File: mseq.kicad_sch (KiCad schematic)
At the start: 63 parts, among them J1 Conn_01x04_Pin, J2 TC2030-NL, P1 USB_C_Plug_USB2.0, SW1 SW_SPST, SW2 BOOT, SW3 RESET, SW4 SW_SPST, U2 SN74AHCT125DR, U3 MIC5219-3.3YM5, U4 CP2102N-Axx-xQFN20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

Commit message: MPN added
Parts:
- C20: footprint Capacitor_SMD:C_0201_0603Metric -> Capacitor_SMD:C_0603_1608Metric; MPN (none) -> KGM15BR71A105JT; voltage rating (none) -> 10
- C4: footprint Capacitor_SMD:C_0201_0603Metric -> Capacitor_SMD:C_0603_1608Metric; MPN (none) -> 0603ZC104JAT2A; Voltage (none) -> 10
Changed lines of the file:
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@@
 			)
 		)
-		(property "Footprint" "Capacitor_SMD:C_0201_0603Metric"
+		(property "Footprint" "Capacitor_SMD:C_0603_1608Metric"
 			(at 97.4852 212.09 0)
 			(effects
@@
 			)
 		)
+		(property "MPN" "0603ZC104JAT2A "
+			(at 96.52 208.28 0)
+			(effects
+				(font
+					(size 1.27 1.27)
+				)
+				(hide yes)
+			)
+		)
+		(property "Voltage" "10"
+			(at 96.52 208.28 0)
+			(effects
+				(font
+					(size 1.27 1.27)
+				)
+				(hide yes)
+			)
+		)
 		(pin "1"
 		)
@@
 			)
 		)
-		(property "Footprint" "Capacitor_SMD:C_0201_0603Metric"
+		(property "Footprint" "Capacitor_SMD:C_0603_1608Metric"
 			(at 86.0552 212.09 0)
 			(effects
@@
 			(at 85.09 208.28 0)
 			(effects
+				(font
+					(size 1.27 1.27)
+				)
+				(hide yes)
+			)
+		)
+		(property "MPN" "KGM15BR71A105JT "
+			(at 85.09 208.28 0)
+			(effects
+				(font
+					(size 1.27 1.27)
+				)
+				(hide yes)
+			)
+		)
+		(property "voltage rating" "10"
+			(at 85.09 208.28 0)
+			(effects

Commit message: MPN capacitor almost done
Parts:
- removed U3: MIC5219-3.3YM5, Package_TO_SOT_SMD:SOT-23-5, symbol Regulator_Linear:MIC5219-3.3YM5
- added U3: MCP1703Ax-330xxTT, Package_TO_SOT_SMD:SOT-23, symbol Regulator_Linear:MCP1703Ax-330xxTT
- C1, C10, C11, C14, C2, C3, C5, C8: footprint Capacitor_SMD:C_0201_0603Metric -> Capacitor_SMD:C_0603_1608Metric; MPN (none) -> 0603ZC104JAT2A; Voltage (none) -> 10
- C21: footprint Capacitor_SMD:C_0201_0603Metric -> Capacitor_SMD:C_0603_1608Metric; MPN (none) -> KAF15AR71H103JM; Voltage (none) -> 50
- C6, C7: value 4.7uF -> 1uF
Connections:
- net BOOT0: now also C8.1; no longer C8.2
- net GND: now also C11.1, C5.2, C8.2, U3.1 (GND); no longer C11.2, C5.1, C8.1
- net NRST: now also C11.2; no longer C5.2
- net VBAT: now also U3.2 (VO)
- net VBUS: now also U3.3 (VI)
- net VDD3: now also C5.1; no longer C11.1
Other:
- moved on the sheet: C7, C9

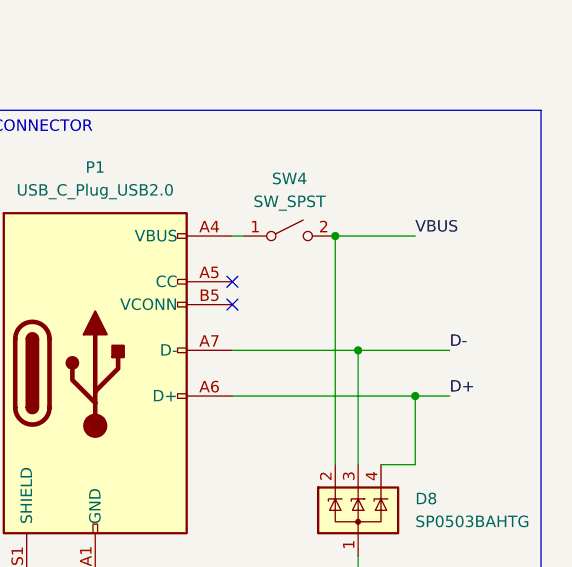
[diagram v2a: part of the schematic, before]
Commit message: Bypass capacitor in VCC don
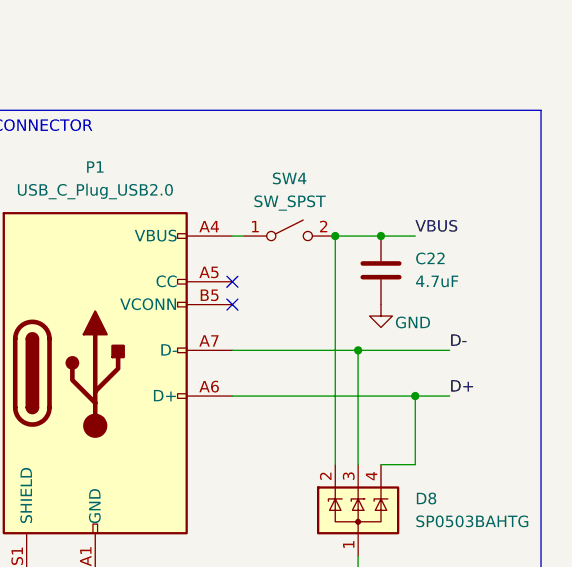
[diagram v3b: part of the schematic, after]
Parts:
- added C22: 4.7uF, Capacitor_SMD:C_0201_0603Metric, symbol Device:C
- C7: footprint Capacitor_SMD:C_0201_0603Metric -> Capacitor_SMD:C_0603_1608Metric; MPN (none) -> KGM15BR71C105JT; Voltage (none) -> 16
- C9: footprint Capacitor_SMD:C_0201_0603Metric -> Capacitor_SMD:C_0603_1608Metric; MPN (none) -> KGM15AR71C103JT; Voltage (none) -> 16
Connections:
- net GND: now also C22.2
- net VBUS: now also C22.1
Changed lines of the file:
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@@
 	)
 	(junction
+		(at 387.35 200.66)
+		(diameter 0)
+		(color 0 0 0 0)
+	)
+	(junction
 		(at 220.98 212.09)
 		(diameter 0)
@@
 	(wire
 		(pts
-			(xy 382.27 200.66) (xy 391.16 200.66)
+			(xy 382.27 200.66) (xy 387.35 200.66)
 		)
 		(stroke
@@
 	(wire
 		(pts
+			(xy 387.35 200.66) (xy 391.16 200.66)
+		)
+		(stroke
+			(width 0)
+			(type default)
+		)
+	)
+	(wire
+		(pts
 			(xy 46.99 160.02) (xy 58.42 160.02)
 		)
@@
 	)
 	(symbol
+		(lib_id "Device:C")
+		(at 387.35 204.47 0)
+		(unit 1)
+		(exclude_from_sim no)
+		(in_bom yes)
+		(on_board yes)
+		(dnp no)
+		(property "Reference" "C22"
+			(at 391.16 203.1999 0)
+			(effects
+				(font
+					(size 1.27 1.27)
+				)
+				(justify left)
+			)
+		)
+		(property "Value" "4.7uF"
+			(at 391.16 205.7399 0)
+			(effects
+				(font
+					(size 1.27 1.27)
+				)
+				(justify left)
+			)
+		)
+		(property "Footprint" "Capacitor_SMD:C_0201_0603Metric"
+			(at 388.3152 208.28 0)
+			(effects
+				(font
+					(size 1.27 1.27)
+				)
+				(hide yes)
+			)
+		)
+		(property "Datasheet" "~"
+			(at 387.35 204.47 0)
+			(effects
+				(font
+					(size 1.27 1.27)
+				)
+				(hide yes)
+			)
+		)
+		(property "Description" "Unpolarized capacitor"
+			(at 387.35 204.47 0)
+			(effects
+				(font
+					(size 1.27 1.27)
+				)
+				(hide yes)
+			)
+		)
+		(pin "1"
+		)
+		(pin "2"
+		)
+		(instances
+			(project "mseq"
+				(path "/4f5593bf-962d-4fa9-909b-449bd6b94d0f"
+					(reference "C22")
+					(unit 1)
+				)
+			)
+		)
+	)
+	(symbol
 		(lib_id "power:GND")
 		(at 330.2 193.04 0)
@@
 			)
 		)
-		(property "Footprint" "Capacitor_SMD:C_0201_0603Metric"
+		(property "Footprint" "Capacitor_SMD:C_0603_1608Metric"
 			(at 47.9552 171.45 0)
 			(effects
@@
 			)
 		)
+		(property "MPN" "KGM15BR71C105JT "
+			(at 46.99 167.64 0)
+			(effects
+				(font
+					(size 1.27 1.27)
+				)
+				(hide yes)
+			)
+		)
+		(property "Voltage" "16"
+			(at 46.99 167.64 0)
+			(effects
+				(font
+					(size 1.27 1.27)
+				)
+				(hide yes)
+			)
+		)
 		(pin "1"
 		)
@@
 	)
 	(symbol
+		(lib_id "power:GND")
+		(at 387.35 208.28 0)
+		(unit 1)
+		(exclude_from_sim no)
+		(in_bom yes)
+		(on_board yes)
+		(dnp no)
+		(property "Reference" "#PWR023"
+			(at 387.35 214.63 0)
+			(effects
+				(font
+					(size 1.27 1.27)
+				)
+				(hide yes)
+			)
+		)
+		(property "Value" "GND"
+			(at 390.906 210.312 0)
+			(effects
+				(font
+					(size 1.27 1.27)
+				)
+			)
+		)
+		(property "Footprint" ""
+			(at 387.35 208.28 0)
+			(effects
+				(font
+					(size 1.27 1.27)
+				)
+				(hide yes)
+			)
+		)
+		(property "Datasheet" ""
+			(at 387.35 208.28 0)
+			(effects
+				(font
+					(size 1.27 1.27)
+				)
+				(hide yes)
+			)
+		)
+		(property "Description" "Power symbol creates a global label with name \"GND\" , ground"
+			(at 387.35 208.28 0)
+			(effects
+				(font
+					(size 1.27 1.27)
+				)
+				(hide yes)
+			)
+		)
+		(pin "1"
+		)
+		(instances
+			(project "mseq"
+				(path "/4f5593bf-962d-4fa9-909b-449bd6b94d0f"
+					(reference "#PWR023")
+					(unit 1)
+				)
+			)
+		)
+	)
+	(symbol
 		(lib_id "Device:R")
 		(at 140.97 251.46 180)
@@
 			)
 		)
-		(property "Footprint" "Capacitor_SMD:C_0201_0603Metric"
+		(property "Footprint" "Capacitor_SMD:C_0603_1608Metric"
 			(at 59.3852 171.45 0)
 			(effects
@@
 			(at 58.42 167.64 0)
 			(effects
+				(font
+					(size 1.27 1.27)
+				)
+				(hide yes)
+			)
+		)
+		(property "MPN" "KGM15AR71C103JT "
+			(at 58.42 167.64 0)
+			(effects
+				(font
+					(size 1.27 1.27)
+				)
+				(hide yes)
+			)
+		)
+		(property "Voltage" "16"
+			(at 58.42 167.64 0)
+			(effects

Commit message: MPN almost done
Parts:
- C12, C6: footprint Capacitor_SMD:C_0201_0603Metric -> Capacitor_SMD:C_0805_2012Metric; MPN (none) -> 08053C105JAT2A; Voltage (none) -> 25
- C13: footprint Capacitor_SMD:C_0201_0603Metric -> Capacitor_SMD:C_0603_1608Metric; MPN (none) -> 06033D104JAT2A; Voltage (none) -> 25
- C14: MPN 0603ZC104JAT2A -> 0603ZC104JAT2A
- C21: MPN KAF15AR71H103JM -> KAF15AR71H103JM
- C22: footprint Capacitor_SMD:C_0201_0603Metric -> Capacitor_SMD:C_1206_3216Metric; MPN (none) -> 12063C475JAT2A; Voltage (none) -> 25
- C7: MPN KGM15BR71C105JT -> KGM15BR71C105JT
- C9: MPN KGM15AR71C103JT -> KGM15AR71C103JT
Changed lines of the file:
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@@
 	)
 	(junction
+		(at 353.06 60.96)
+		(diameter 0)
+		(color 0 0 0 0)
+	)
+	(junction
 		(at 58.42 160.02)
 		(diameter 0)
@@
 	)
 	(junction
+		(at 353.06 53.34)
+		(diameter 0)
+		(color 0 0 0 0)
+	)
+	(junction
 		(at 135.89 246.38)
 		(diameter 0)
@@
 	)
 	(junction
-		(at 353.06 53.34)
-		(diameter 0)
-		(color 0 0 0 0)
-	)
-	(junction
 		(at 391.16 218.44)
 		(diameter 0)
@@
 		(color 0 0 0 0)
 	)
-	(junction
-		(at 353.06 60.96)
-		(diameter 0)
-		(color 0 0 0 0)
-	)
 	(no_connect
 		(at 31.75 102.87)
@@
 	(wire
 		(pts
-			(xy 353.06 53.34) (xy 364.49 53.34)
-		)
-		(stroke
-			(width 0)
-			(type default)
-		)
-	)
-	(wire
-		(pts
 			(xy 144.78 194.31) (xy 144.78 195.58)
 		)
@@
 	(wire
 		(pts
+			(xy 353.06 53.34) (xy 364.49 53.34)
+		)
+		(stroke
+			(width 0)
+			(type default)
+		)
+	)
+	(wire
+		(pts
 			(xy 54.61 212.09) (xy 54.61 213.36)
 		)
@@
 			)
 		)
-		(property "Footprint" "Capacitor_SMD:C_0201_0603Metric"
+		(property "Footprint" "Capacitor_SMD:C_1206_3216Metric"
 			(at 388.3152 208.28 0)
 			(effects
@@
 			)
 		)
+		(property "MPN" "12063C475JAT2A"
+			(at 387.35 204.47 0)
+			(effects
+				(font
+					(size 1.27 1.27)
+				)
+				(hide yes)
+			)
+		)
+		(property "Voltage" "25"
+			(at 387.35 204.47 0)
+			(effects
+				(font
+					(size 1.27 1.27)
+				)
+				(hide yes)
+			)
+		)
 		(pin "1"
 		)
@@
 			)
 		)
-		(property "Footprint" "Capacitor_SMD:C_0201_0603Metric"
+		(property "Footprint" "Capacitor_SMD:C_0603_1608Metric"
 			(at 365.4552 60.96 0)
 			(effects
@@
 			)
 		)
+		(property "MPN" "06033D104JAT2A"
+			(at 364.49 57.15 0)
+			(effects
+				(font
+					(size 1.27 1.27)
+				)
+				(hide yes)
+			)
+		)
+		(property "Voltage" "25"
+			(at 364.49 57.15 0)
+			(effects
+				(font
+					(size 1.27 1.27)
+				)
+				(hide yes)
+			)
+		)
 		(pin "1"
 		)
@@
 	)
 	(symbol
+		(lib_id "Device:C")
+		(at 353.06 57.15 0)
+		(unit 1)
+		(exclude_from_sim no)
+		(in_bom yes)
+		(on_board yes)
+		(dnp no)
+		(property "Reference" "C12"
+			(at 356.87 55.8799 0)
+			(effects
+				(font
+					(size 1.27 1.27)
+				)
+				(justify left)
+			)
+		)
+		(property "Value" "1uF"
+			(at 356.87 58.4199 0)
+			(effects
+				(font
+					(size 1.27 1.27)
+				)
+				(justify left)
+			)
+		)
+		(property "Footprint" "Capacitor_SMD:C_0805_2012Metric"
+			(at 354.0252 60.96 0)
+			(effects
+				(font
+					(size 1.27 1.27)
+				)
+				(hide yes)
+			)
+		)
+		(property "Datasheet" "~"
+			(at 353.06 57.15 0)
+			(effects
+				(font
+					(size 1.27 1.27)
+				)
+				(hide yes)
+			)
+		)
+		(property "Description" "Unpolarized capacitor"
+			(at 353.06 57.15 0)
+			(effects
+				(font
+					(size 1.27 1.27)
+				)
+				(hide yes)
+			)
+		)
+		(property "MPN" "08053C105JAT2A"
+			(at 353.06 57.15 0)
+			(effects
+				(font
+					(size 1.27 1.27)
+				)
+				(hide yes)
+			)
+		)
+		(property "Voltage" "25"
+			(at 353.06 57.15 0)
+			(effects
+				(font
+					(size 1.27 1.27)
+				)
+				(hide yes)
+			)
+		)
+		(pin "1"
+		)
+		(pin "2"
+		)
+		(instances
+			(project "mseq"
+				(path "/4f5593bf-962d-4fa9-909b-449bd6b94d0f"
+					(reference "C12")
+					(unit 1)
+				)
+			)
+		)
+	)
+	(symbol
 		(lib_id "Device:FerriteBead")
 		(at 86.36 73.66 270)
@@
 			)
 		)
-		(property "Footprint" "Capacitor_SMD:C_0201_0603Metric"
+		(property "Footprint" "Capacitor_SMD:C_0805_2012Metric"
 			(at 23.8252 171.45 0)
 			(effects
@@
 			)
 		)
+		(property "MPN" "08053C105JAT2A"
+			(at 22.86 167.64 0)
+			(effects
+				(font
+					(size 1.27 1.27)
+				)
+				(hide yes)
+			)
+		)
+		(property "Voltage" "25"
+			(at 22.86 167.64 0)
+			(effects
+				(font
+					(size 1.27 1.27)
+				)
+				(hide yes)
+			)
+		)
 		(pin "1"
 		)
@@
 	(symbol
 		(lib_id "Device:C")
-		(at 353.06 57.15 0)
-		(unit 1)
-		(exclude_from_sim no)
-		(in_bom yes)
-		(on_board yes)
-		(dnp no)
-		(property "Reference" "C12"
-			(at 356.87 55.8799 0)
-			(effects
-				(font
-					(size 1.27 1.27)
-				)
-				(justify left)
-			)
-		)
-		(property "Value" "1uF"
-			(at 356.87 58.4199 0)
-			(effects
-				(font
-					(size 1.27 1.27)
-				)
-				(justify left)
-			)
-		)
-		(property "Footprint" "Capacitor_SMD:C_0201_0603Metric"
-			(at 354.0252 60.96 0)
-			(effects
-				(font
-					(size 1.27 1.27)
-				)
-				(hide yes)
-			)
-		)
-		(property "Datasheet" "~"
-			(at 353.06 57.15 0)
-			(effects
-				(font
-					(size 1.27 1.27)
-				)
-				(hide yes)
-			)
-		)
-		(property "Description" "Unpolarized capacitor"
-			(at 353.06 57.15 0)
-			(effects
-				(font
-					(size 1.27 1.27)
-				)
-				(hide yes)
-			)
-		)
-		(pin "1"
-		)
-		(pin "2"
-		)
-		(instances
-			(project "mseq"
-				(path "/4f5593bf-962d-4fa9-909b-449bd6b94d0f"
-					(reference "C12")
-					(unit 1)
-				)
-			)
-		)
-	)
-	(symbol
-		(lib_id "Device:C")
 		(at 43.18 208.28 0)
 		(unit 1)
@@
 			)
 		)
-		(property "MPN" "KAF15AR71H103JM "
+		(property "MPN" "KAF15AR71H103JM"
 			(at 62.23 72.39 0)
 			(effects
@@
 			)
 		)
-		(property "MPN" "KGM15BR71C105JT "
+		(property "MPN" "KGM15BR71C105JT"
 			(at 46.99 167.64 0)
 			(effects
@@
 			)
 		)
-		(property "MPN" "0603ZC104JAT2A "
+		(property "MPN" "0603ZC104JAT2A"
 			(at 121.92 76.2 0)
 			(effects
@@
 			)
 		)
-		(property "MPN" "KGM15AR71C103JT "
+		(property "MPN" "KGM15AR71C103JT"
 			(at 58.42 167.64 0)
 			(effects

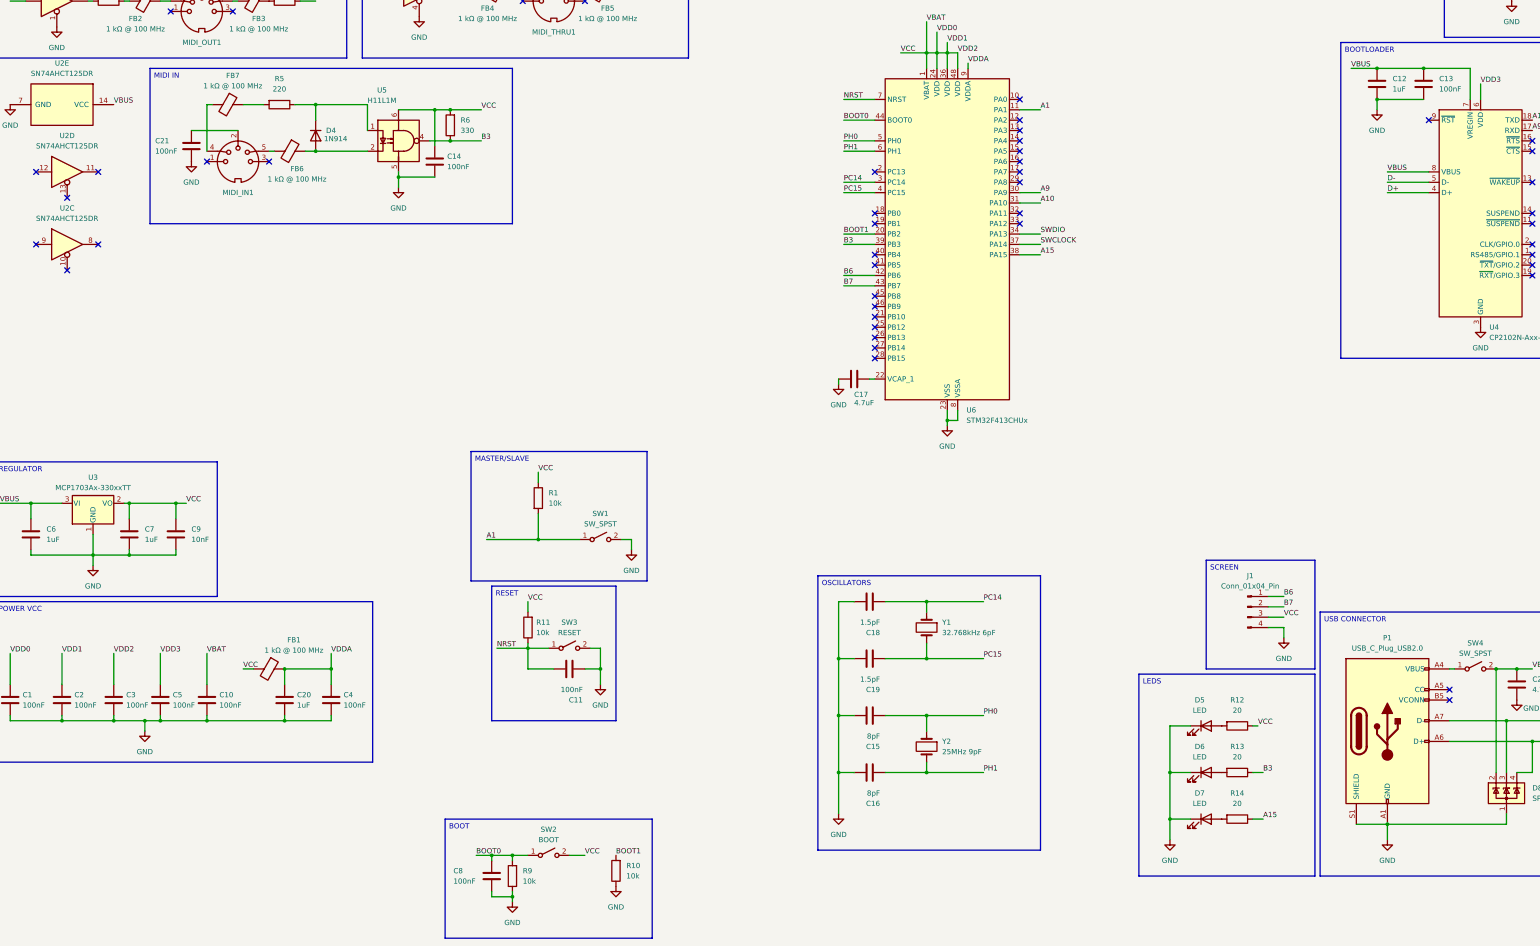
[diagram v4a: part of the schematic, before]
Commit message: MPN for bypass capacitors done
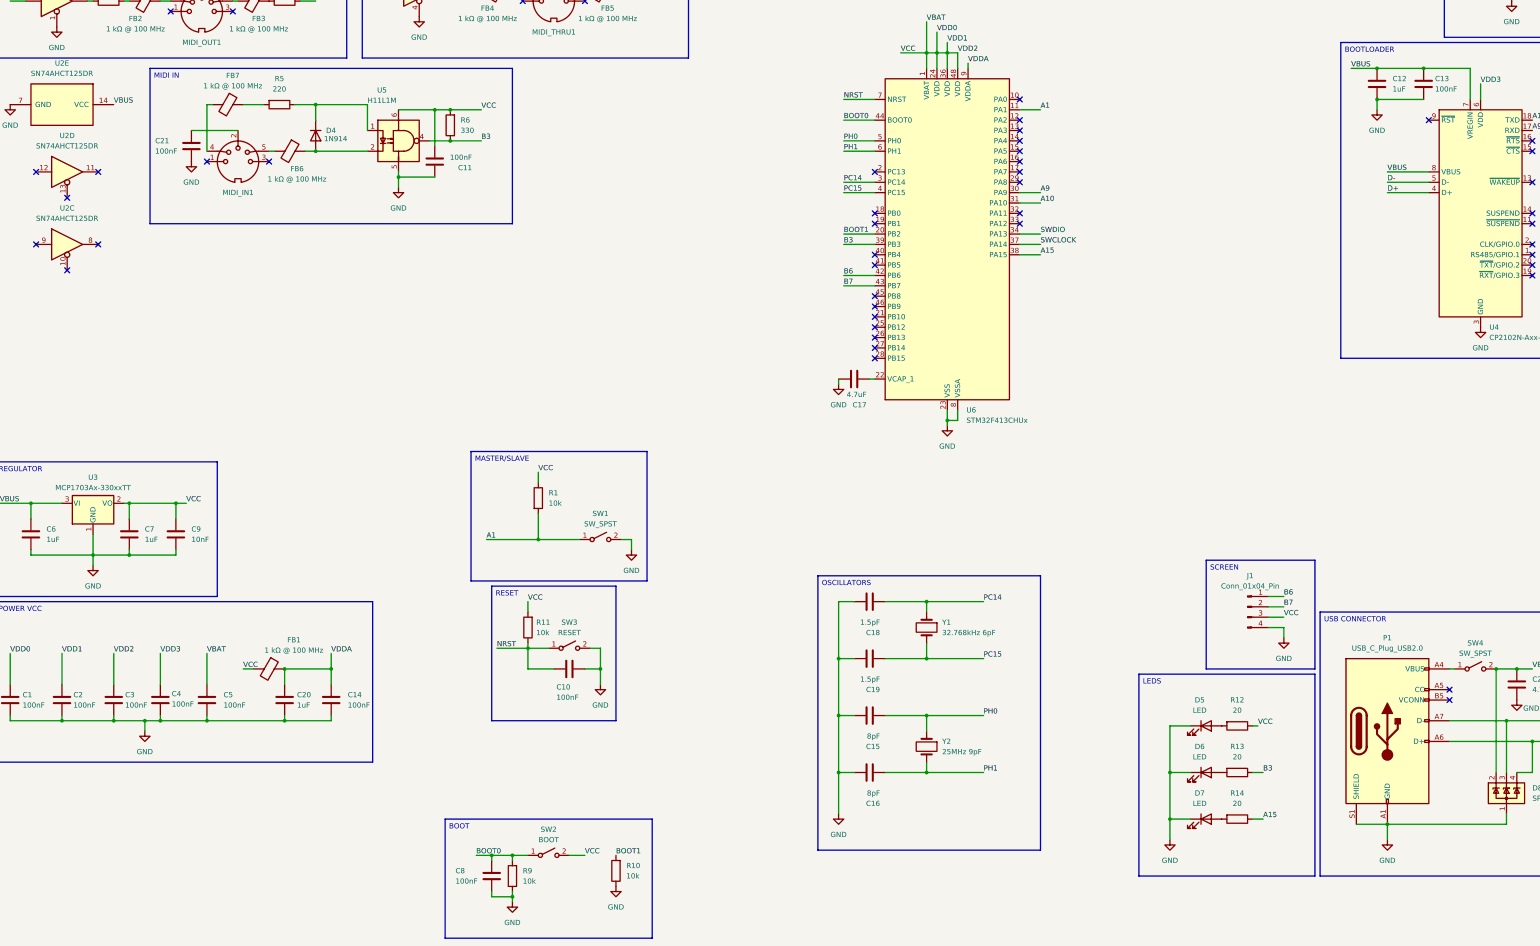
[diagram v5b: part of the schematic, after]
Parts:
- C1, C10, C11, C14, C2, C3, C4, C5, C8: MPN 0603ZC104JAT2A -> 06035C104JAT2A; Voltage 10 -> 50
- C12, C6: MPN 08053C105JAT2A -> KGM21AR71E105JU
- C13: MPN 06033D104JAT2A -> 06035C104JAT2A; Voltage 25 -> 50
- C17: footprint Capacitor_SMD:C_0201_0603Metric -> Capacitor_SMD:C_1206_3216Metric; MPN (none) -> 12063C475JAT2A; Voltage (none) -> 25
- C21: MPN KAF15AR71H103JM -> 06035C104JAT2A
- C7: footprint Capacitor_SMD:C_0603_1608Metric -> Capacitor_SMD:C_0805_2012Metric; MPN KGM15BR71C105JT -> KGM21AR71E105JU; Voltage 16 -> 25
- C9: MPN KGM15AR71C103JT -> 06035C103JAT2A; Voltage 16 -> 50
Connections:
- net GND: now also C11.2, C13.1; no longer C11.1, C13.2
- net NRST: now also C10.1; no longer C11.2
- net VBAT: now also C11.1, C5.1; no longer C10.1, C14.1
- net VBUS: now also C13.2; no longer C13.1
- net VDD3: now also C4.1; no longer C5.1
- net VDDA: now also C14.1; no longer C4.1
